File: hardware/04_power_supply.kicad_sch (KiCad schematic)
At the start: 10 parts, among them U4 LMR16006XDDCR

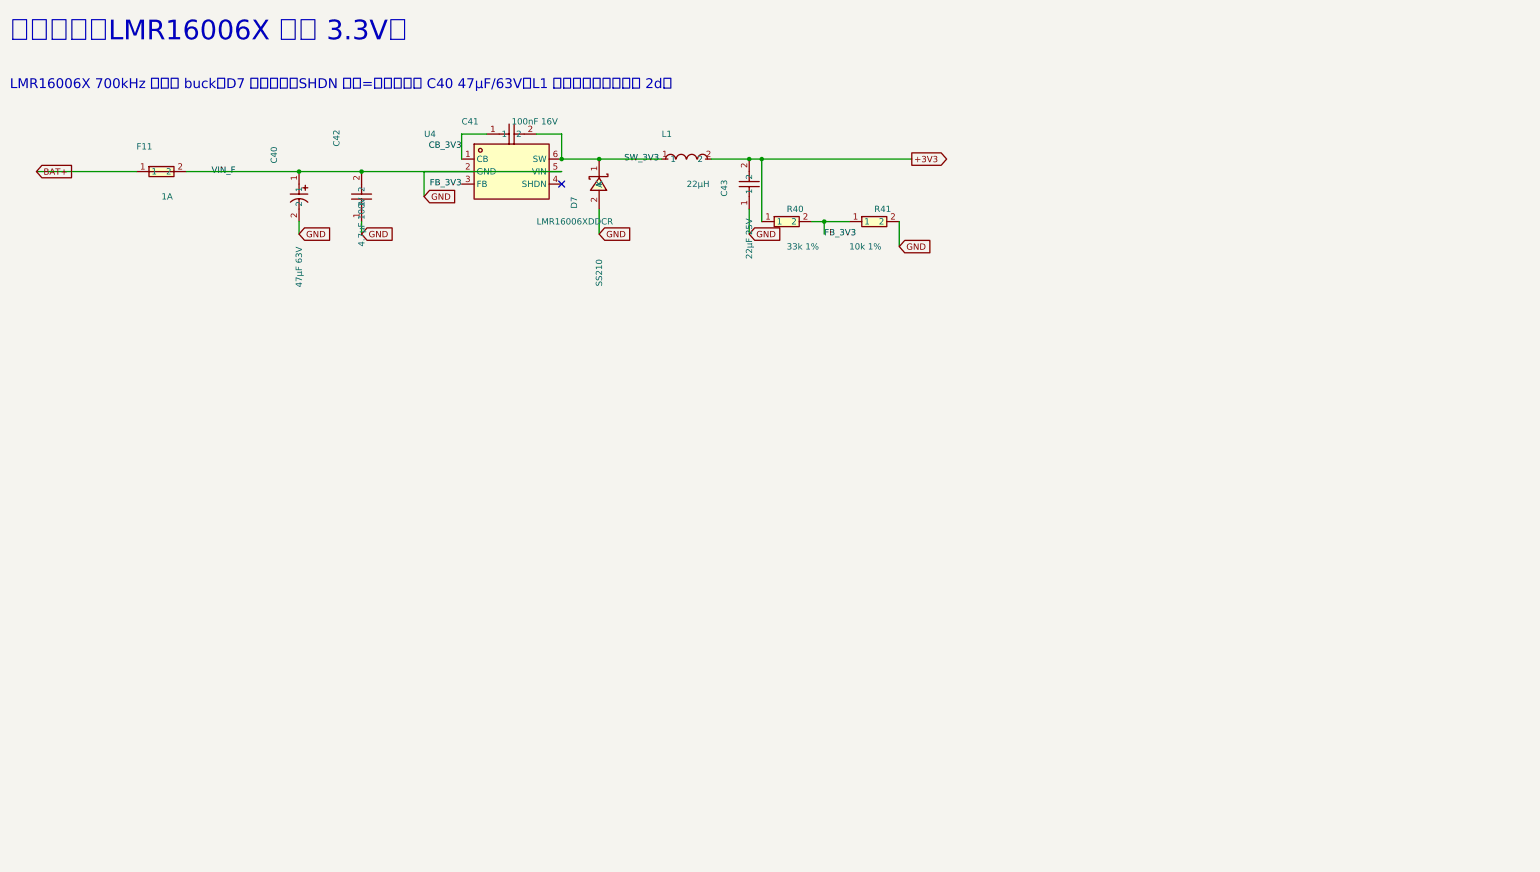
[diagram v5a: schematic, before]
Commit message: 04 子图第 3 轮：版面返工（标签引出、分组、文字不重叠，8 项自检通过）；取库 R42 10Ω 1206 C17903；第 4 轮任务书（P0 Footprint 字段、P1 输入串 10Ω）
Co-Authored-By: Claude Opus 5.5 <noreply@anthropic.com>
Claude-Session: https://claude.ai/code/session_018LcBBXJnjJ1MVmds7Fkezv
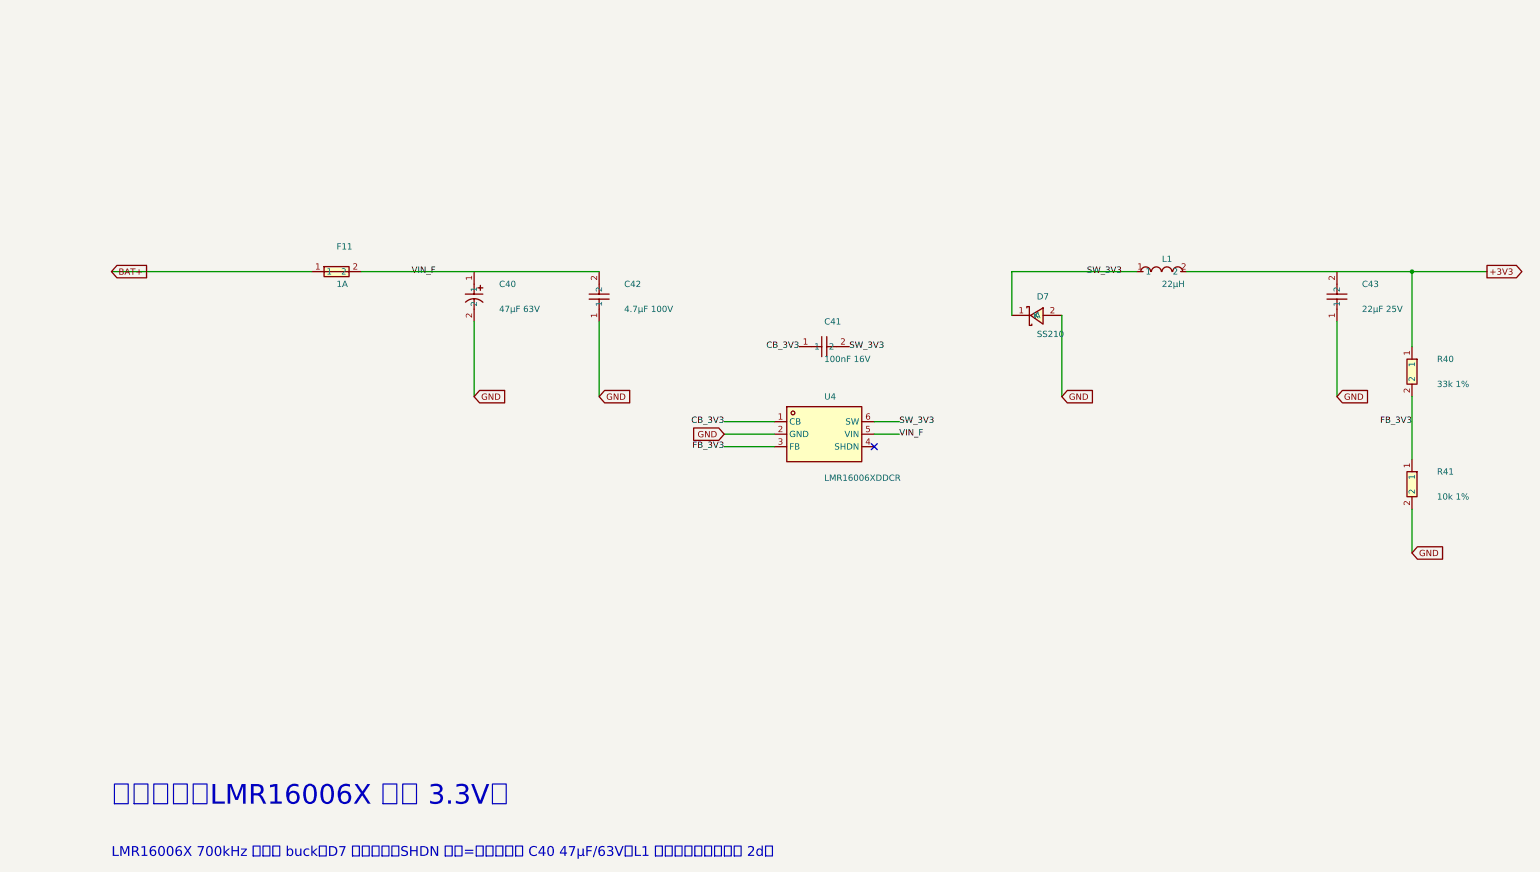
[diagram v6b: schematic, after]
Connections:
- net GND: no longer C40.1, C42.2, F11.2, U4.5 (VIN)
- new net VIN_F: C40.1, C42.2, F11.2, U4.5 (VIN)
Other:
- moved on the sheet: C40, C41, C42, C43, D7, F11, L1, R40, R41, U4
